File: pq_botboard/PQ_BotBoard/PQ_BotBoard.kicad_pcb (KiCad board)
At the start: 6 copper layers, 64 x 52 mm, 37 parts, among them IC1 TCN75AVOA713, J1 53261-1471, J2 Conn_01x08_MountingPin, J5 Conn_01x03_MountingPin, U1 TPS7A7002DDAR

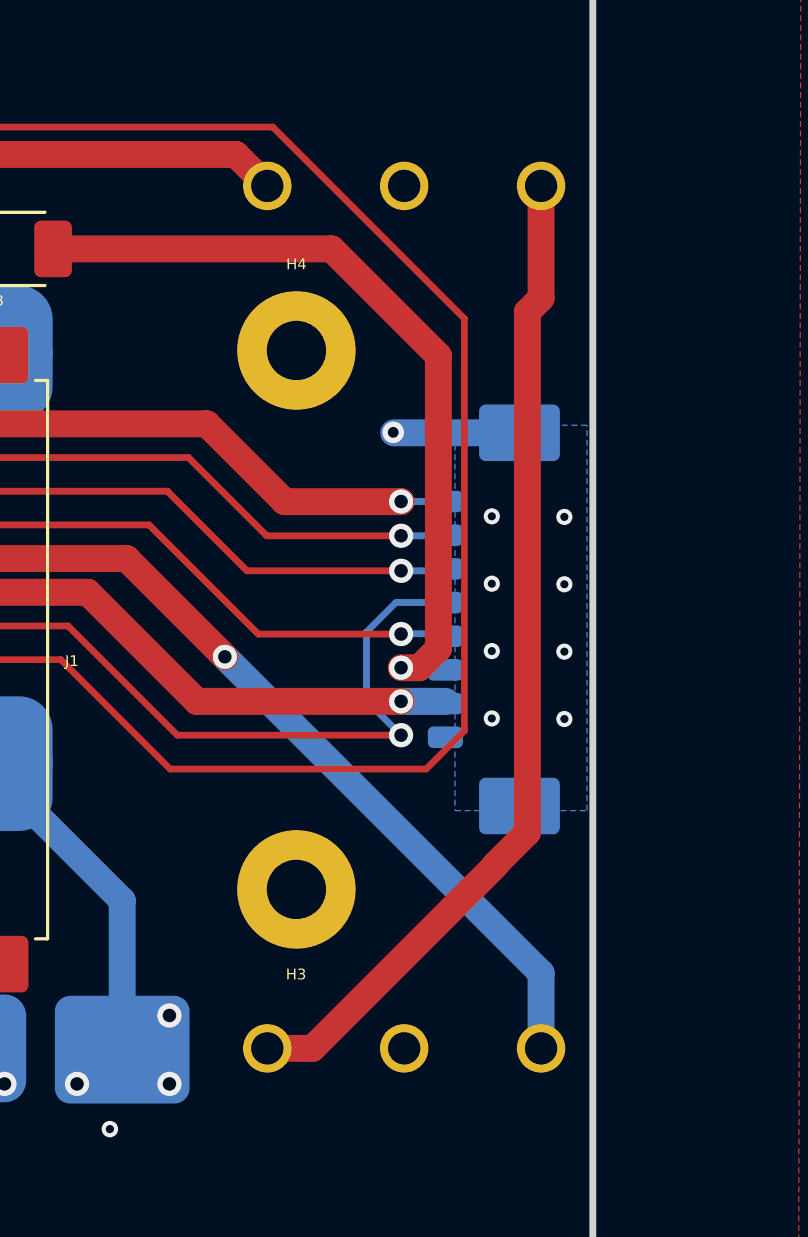
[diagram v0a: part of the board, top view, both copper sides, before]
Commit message: adjust killswitches holes to better align bottom with slider deployer PCB
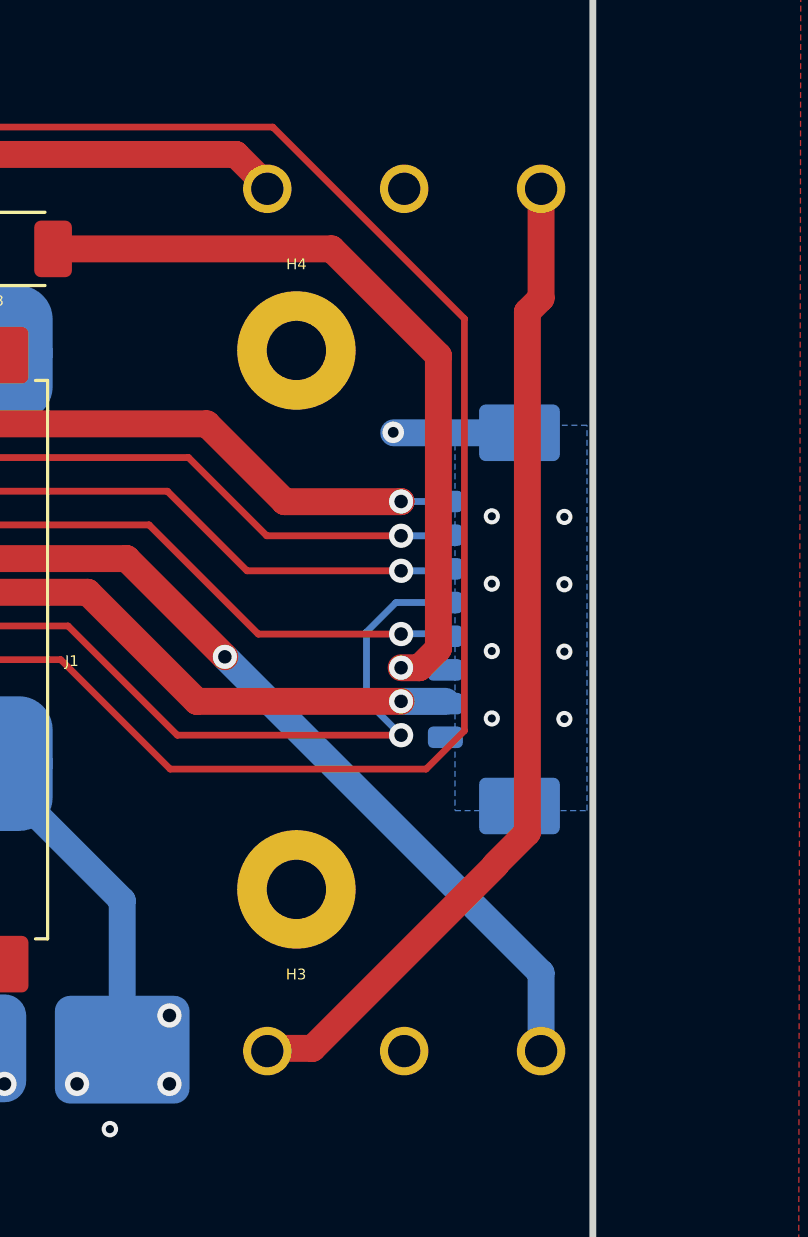
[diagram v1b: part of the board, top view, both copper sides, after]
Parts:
- moved KS1 0.11 mm to (121.9, 41.0)
- moved KS2 0.10 mm to (121.9, 73.0)
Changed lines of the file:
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@@
   )
   (footprint "miscelaneous-nsl:D2FLA" (layer "B.Cu")
-    (at 121.92 72.8996)
+    (at 121.92 73)
     (descr "D2F-L-A-3")
     (tags "Switch")
@@
     (attr through_hole)
     (fp_text reference "KS2" (at 5.08 6.45 180 unlocked) (layer "B.SilkS")
-        (effects (font (size 0.4 0.4) (thickness 0.15)) (justify mirror))
+        (effects (font (size 0.4 0.4) (thickness 0.1)) (justify mirror))
     )
     (fp_text value "D2F-01L-A" (at 5.08 6.45 180) (layer "B.SilkS") hide
@@
   )
   (footprint "miscelaneous-nsl:D2FLA1" (layer "B.Cu")
-    (at 121.92 40.894)
+    (at 121.92 41)
     (descr "D2F-L-A1-2")
     (tags "Switch")
@@
     (attr through_hole)
     (fp_text reference "KS1" (at 5.08 -6.45 180 unlocked) (layer "B.SilkS")
-        (effects (font (size 0.4 0.4) (thickness 0.15)) (justify mirror))
+        (effects (font (size 0.4 0.4) (thickness 0.1)) (justify mirror))
     )
     (fp_text value "D2F-01L-A1" (at 5.08 -6.45 180) (layer "B.SilkS") hide
